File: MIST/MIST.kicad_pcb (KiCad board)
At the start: 2 copper layers, 10 x 10 mm, 2 parts

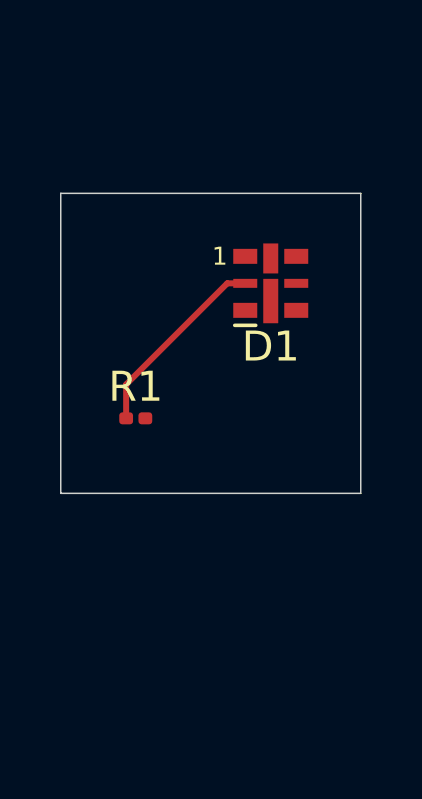
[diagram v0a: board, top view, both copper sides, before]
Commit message: finished BOM and added resources and started layout
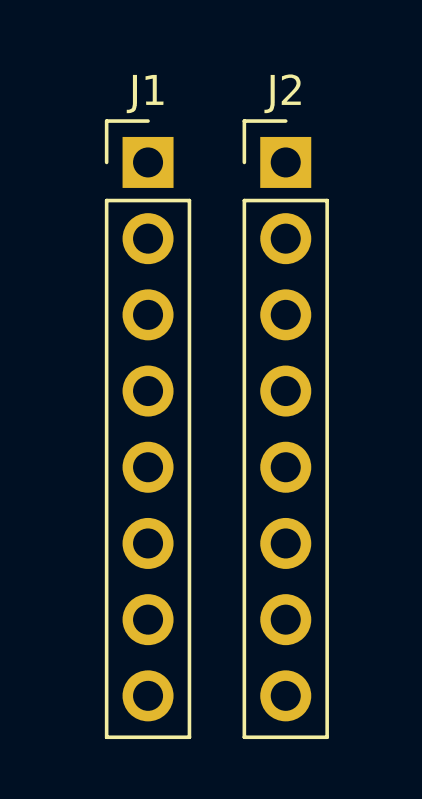
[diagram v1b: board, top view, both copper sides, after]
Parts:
- removed D1: LED, LED_SMD:LED-APA102-2020
- removed R1: 220, Resistor_SMD:R_0201_0603Metric
- added J1: Conn_01x08, Connector_PinHeader_2.54mm:PinHeader_1x08_P2.54mm_Vertical, F.Cu at (140.9, 88.0)
- added J2: Conn_01x08, Connector_PinHeader_2.54mm:PinHeader_1x08_P2.54mm_Vertical, F.Cu at (145.5, 88.0)
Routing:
- net /LED_Anode: track 6.50 -> 0.00 mm
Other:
- board outline removed

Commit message: finished schematic. updated BOM. stuff.
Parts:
- added C1: 100n, Capacitor_SMD:C_0805_2012Metric, F.Cu at (163.8, 39.0)
- added C2: 100n, Capacitor_SMD:C_0805_2012Metric, F.Cu at (163.8, 42.0)
- added C3: 22pF, Capacitor_SMD:C_0805_2012Metric, F.Cu at (163.8, 45.0)
- added C4: 22pF, Capacitor_SMD:C_0805_2012Metric, F.Cu at (163.8, 48.0)
- added C5: 22uF, Capacitor_SMD:C_0805_2012Metric, F.Cu at (163.8, 51.0)
- added J3: USB_C_Receptacle_PowerOnly_6P, Connector_USB:USB_C_Receptacle_GCT_USB4125-xx-x_6P_TopMnt_Horizontal, F.Cu at (179.0, 57.8)
- added J4: ICSP, Connector_PinHeader_2.54mm:PinHeader_2x03_P2.54mm_Vertical, F.Cu at (156.5, 63.5)
- added MK1: CMC-5042PF-AC, CMC-5042PF-AC:CUI_CMC-5042PF-AC, F.Cu at (138.0, 59.2)
- added R1: 10k, Resistor_SMD:R_1206_3216Metric, F.Cu at (181.0, 38.2)
- added R4: 5.1k, Resistor_SMD:R_1206_3216Metric, F.Cu at (181.0, 41.6)
- added R5: 5.1k, Resistor_SMD:R_1206_3216Metric, F.Cu at (181.0, 44.9)
- added S1: SKRPABE010, SKRPABE010:SW_SKRPABE010, F.Cu at (123.2, 62.8)
- added S2: SKRPABE010, SKRPABE010:SW_SKRPABE010, F.Cu at (123.2, 72.5)
- added U1: ATmega328PB-A, Package_QFP:TQFP-32_7x7mm_P0.8mm, F.Cu at (143.1, 48.4)
- added U3: MAX4466EXK, MAX4466EXK:SOT65P210X110-5N, F.Cu at (137.0, 75.2)
- added Y1: 16 Mhz Crystal, Crystal:Crystal_SMD_3225-4Pin_3.2x2.5mm, F.Cu at (151.7, 36.1)
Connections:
- J1 pad 1: unconnected-(J1-Pin_1-Pad1) -> /COL1 (P13)
- J1 pad 2: unconnected-(J1-Pin_2-Pad2) -> /COL2 (P3)
- J1 pad 3: unconnected-(J1-Pin_3-Pad3) -> /COL3 (P4)
- J1 pad 4: unconnected-(J1-Pin_4-Pad4) -> /COL4 (P10)
- J1 pad 5: unconnected-(J1-Pin_5-Pad5) -> /COL5 (P6)
- J1 pad 6: unconnected-(J1-Pin_6-Pad6) -> /COL6 (P11)
- J1 pad 7: unconnected-(J1-Pin_7-Pad7) -> /COL7 (P15)
- J1 pad 8: unconnected-(J1-Pin_8-Pad8) -> /COL8 (P16)
- J2 pad 1: unconnected-(J2-Pin_1-Pad1) -> /ROW1 (P9)
- J2 pad 2: unconnected-(J2-Pin_2-Pad2) -> /ROW2 (P14)
- J2 pad 3: unconnected-(J2-Pin_3-Pad3) -> /ROW3 (P8)
- J2 pad 4: unconnected-(J2-Pin_4-Pad4) -> /ROW4 (P12)
- J2 pad 5: unconnected-(J2-Pin_5-Pad5) -> /ROW5 (P1)
- J2 pad 6: unconnected-(J2-Pin_6-Pad6) -> /ROW6 (P7)
- J2 pad 7: unconnected-(J2-Pin_7-Pad7) -> /ROW7 (P2)
- J2 pad 8: unconnected-(J2-Pin_8-Pad8) -> /ROW8 (P5)

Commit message: finished schematic and layout
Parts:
- added C6: 0.1u, Capacitor_SMD:C_0805_2012Metric, F.Cu at (195.3, 95.8)
- added C7: 0.1n, Capacitor_SMD:C_0805_2012Metric, F.Cu at (195.3, 99.8)
- added C8: 0.1u, Capacitor_SMD:C_0805_2012Metric, F.Cu at (195.3, 103.8)
- added C9: 0.1u, Capacitor_SMD:C_0805_2012Metric, F.Cu at (172.0, 92.2)
- added G***: LOGO, LOGO, F.Cu at (195.8, 110.5)
- added G***: LOGO, LOGO, B.Cu at (154.5, 99.8)
- added G***: LOGO, LOGO, B.Cu at (199.0, 110.5)
- added G***: LOGO, LOGO, B.Cu at (204.0, 100.5)
- added R10: 100k, Resistor_SMD:R_0805_2012Metric, F.Cu at (189.8, 109.5)
- added R2: 10k, Resistor_SMD:R_0805_2012Metric, F.Cu at (189.8, 89.8)
- added R3: 10k, Capacitor_SMD:C_0805_2012Metric, F.Cu at (176.9, 92.2)
- added R6: 2k, Resistor_SMD:R_0805_2012Metric, F.Cu at (189.8, 93.7)
- added R7: 2k, Resistor_SMD:R_0805_2012Metric, F.Cu at (189.8, 97.8)
- added R8: 1M, Resistor_SMD:R_0805_2012Metric, F.Cu at (189.9, 101.5)
- added R9: 1M, Resistor_SMD:R_0805_2012Metric, F.Cu at (189.9, 105.5)
- added U2: MAX7219, Package_SO:SOIC-24W_7.5x15.4mm_P1.27mm, F.Cu at (174.0, 100.0)
- moved S2 89.9 mm to (205.0, 110.0)
- moved S1 89.8 mm to (205.0, 100.0)
- moved R4 76.9 mm to (147.0, 110.5)
- moved MK1 73.7 mm to (205.0, 90.0)
- moved R5 71.1 mm to (147.0, 107.2)
- moved Y1 65.7 mm to (146.9, 101.7)
- moved C1 64.0 mm to (162.7, 103.0), turned to 180 degrees
- moved J3 63.9 mm to (139.2, 107.8), turned to -90 degrees
- moved U3 60.6 mm to (195.8, 90.0)
- moved R1 59.9 mm to (155.0, 92.2)
- moved C2 58.0 mm to (162.7, 100.0), turned to 180 degrees
- moved C3 54.0 mm to (147.5, 96.5), turned to 90 degrees
- moved U1 52.9 mm to (155.0, 100.0)
- moved C4 52.1 mm to (144.5, 96.5), turned to -90 degrees
- moved C5 44.4 mm to (147.5, 92.3), turned to -90 degrees
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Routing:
- net +5V: track 0.00 -> 117.9 mm, vias 0 -> 10
- net /!RESET: track 0.00 -> 88.9 mm, vias 0 -> 2
- net /SWITCHMODE: track 0.00 -> 62.2 mm
- net /ADC0: track 0.00 -> 57.7 mm, vias 0 -> 3
- net /SCK: track 0.00 -> 55.3 mm, vias 0 -> 2
- net Net-(U3-IN+): track 0.00 -> 47.6 mm, vias 0 -> 2
- net GND: track 0.00 -> 45.2 mm, vias 0 -> 20
- net /MOSI: track 0.00 -> 32.1 mm, vias 0 -> 3
- net /MISO: track 0.00 -> 29.1 mm
- net /SS: track 0.00 -> 29.0 mm, vias 0 -> 2
- net Net-(U3-IN-): track 0.00 -> 28.7 mm, vias 0 -> 3
- net /ROW2 (P14): track 0.00 -> 26.7 mm
- net /COL3 (P4): track 0.00 -> 19.9 mm, vias 0 -> 2
- net /COL2 (P3): track 0.00 -> 16.9 mm
- net /COL8 (P16): track 0.00 -> 16.2 mm
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- added copper zone on F.Cu, net GND
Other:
- board outline added: 75.5 x 30.8 mm
- board text added: "1"
- board text added: "MIST"
- board text added: "Mode 1: Talk with MIST Mode 2: Sound visualizer. Play music to the microphone and watch the lights go"
- board text added: "Orientation -> Pin 1 Here"
- board text added: "Play Music Here!"
- board text added: "Reset"
- board text added: "Switch Mode"

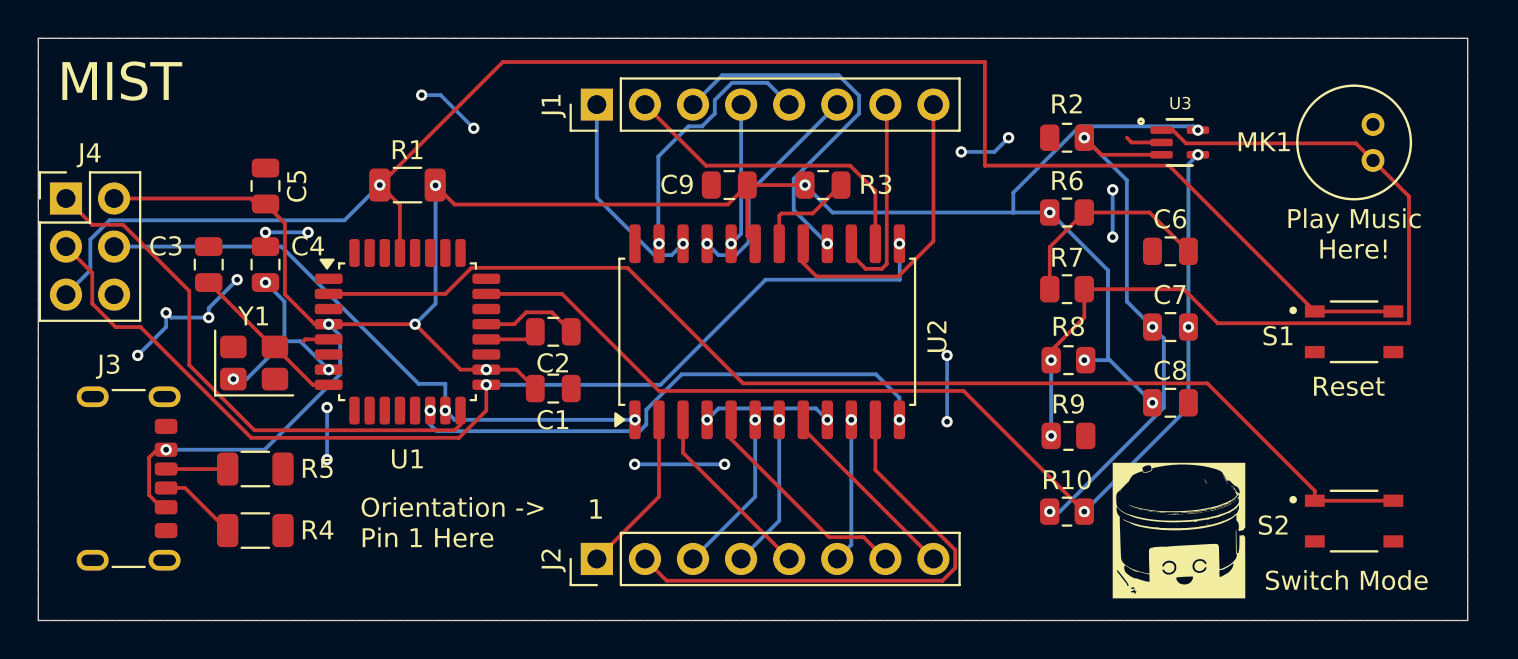
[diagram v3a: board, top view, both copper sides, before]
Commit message: added GND planes to both layers and via stitched
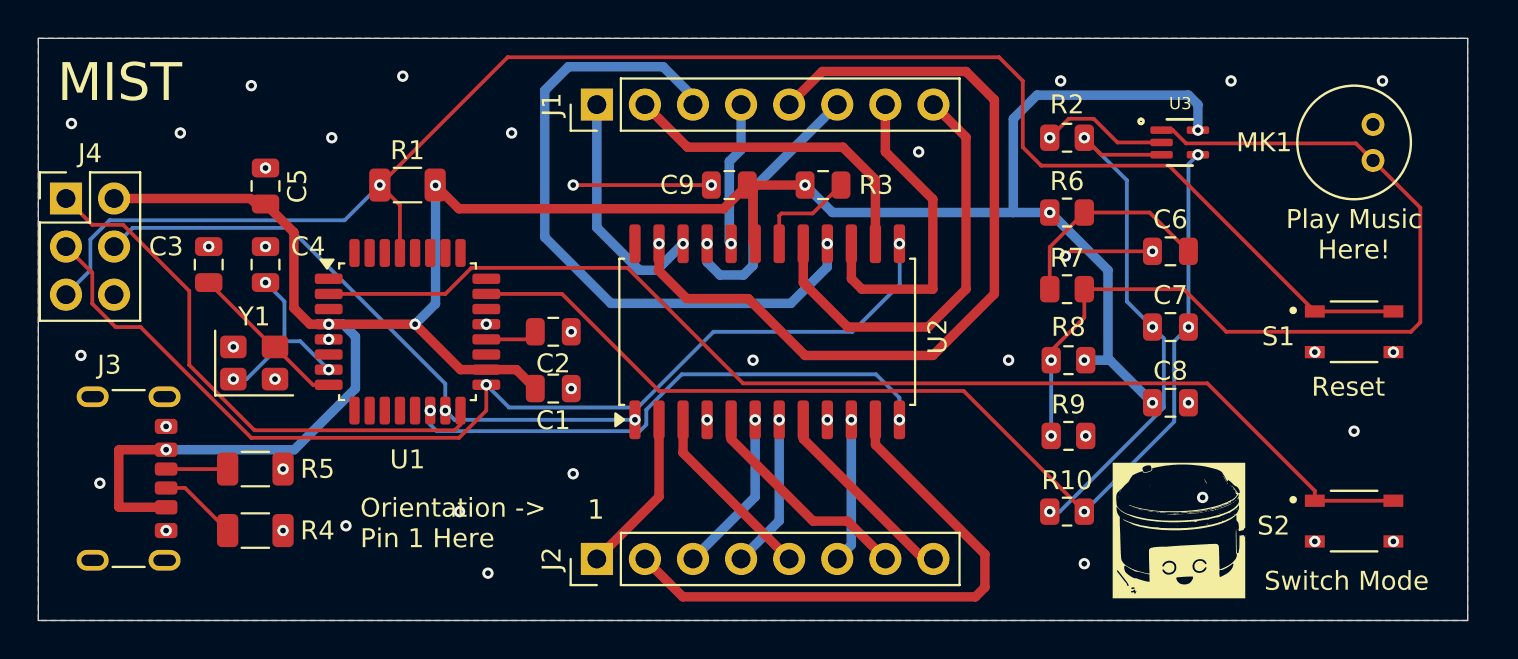
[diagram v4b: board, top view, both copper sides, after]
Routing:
- net /COL5 (P6): track 14.0 -> 44.8 mm
- net GND: track 45.2 -> 18.8 mm, vias 20 -> 53
- net /COL3 (P4): track 19.9 -> 35.6 mm
- net +5V: track 117.9 -> 128.5 mm, vias 10 -> 9
- net /COL8 (P16): track 16.2 -> 22.9 mm
- net /COL7 (P15): track 11.3 -> 17.2 mm
- net /ROW2 (P14): track 26.7 -> 30.2 mm
- net /COL6 (P11): track 11.9 -> 14.2 mm
- net /COL1 (P13): track 11.0 -> 12.6 mm
- net Net-(U3-IN+): track 47.6 -> 48.8 mm
- net /SCK: track 55.3 -> 56.5 mm
- net /!RESET: track 88.9 -> 87.9 mm
- net /MOSI: track 32.1 -> 33.0 mm
- added copper zone on B.Cu, net GND

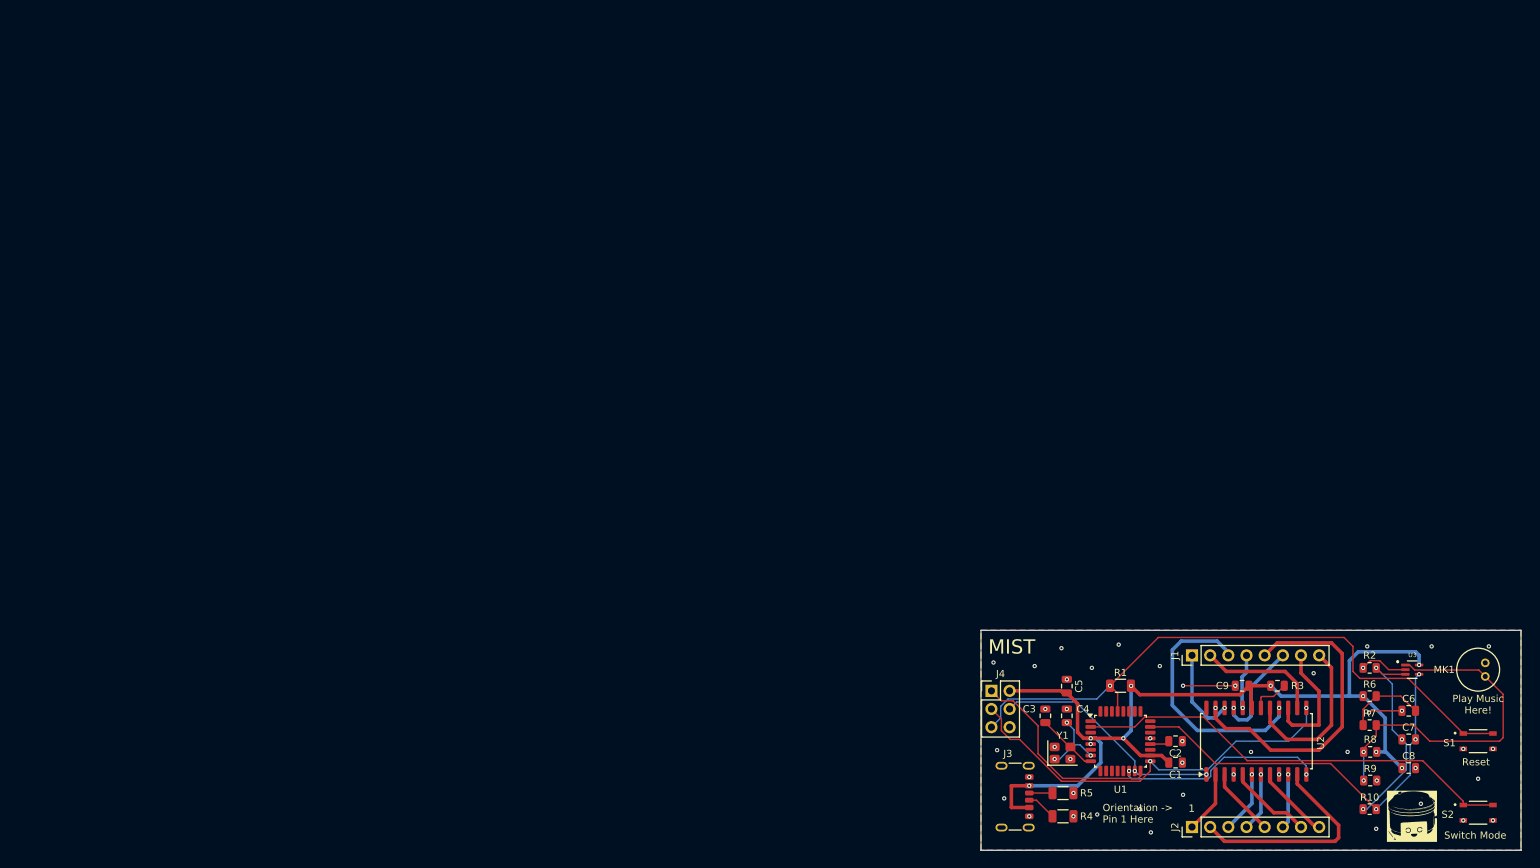
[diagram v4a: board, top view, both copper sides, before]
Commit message: fixed wrong matrix pin mappings schematic.
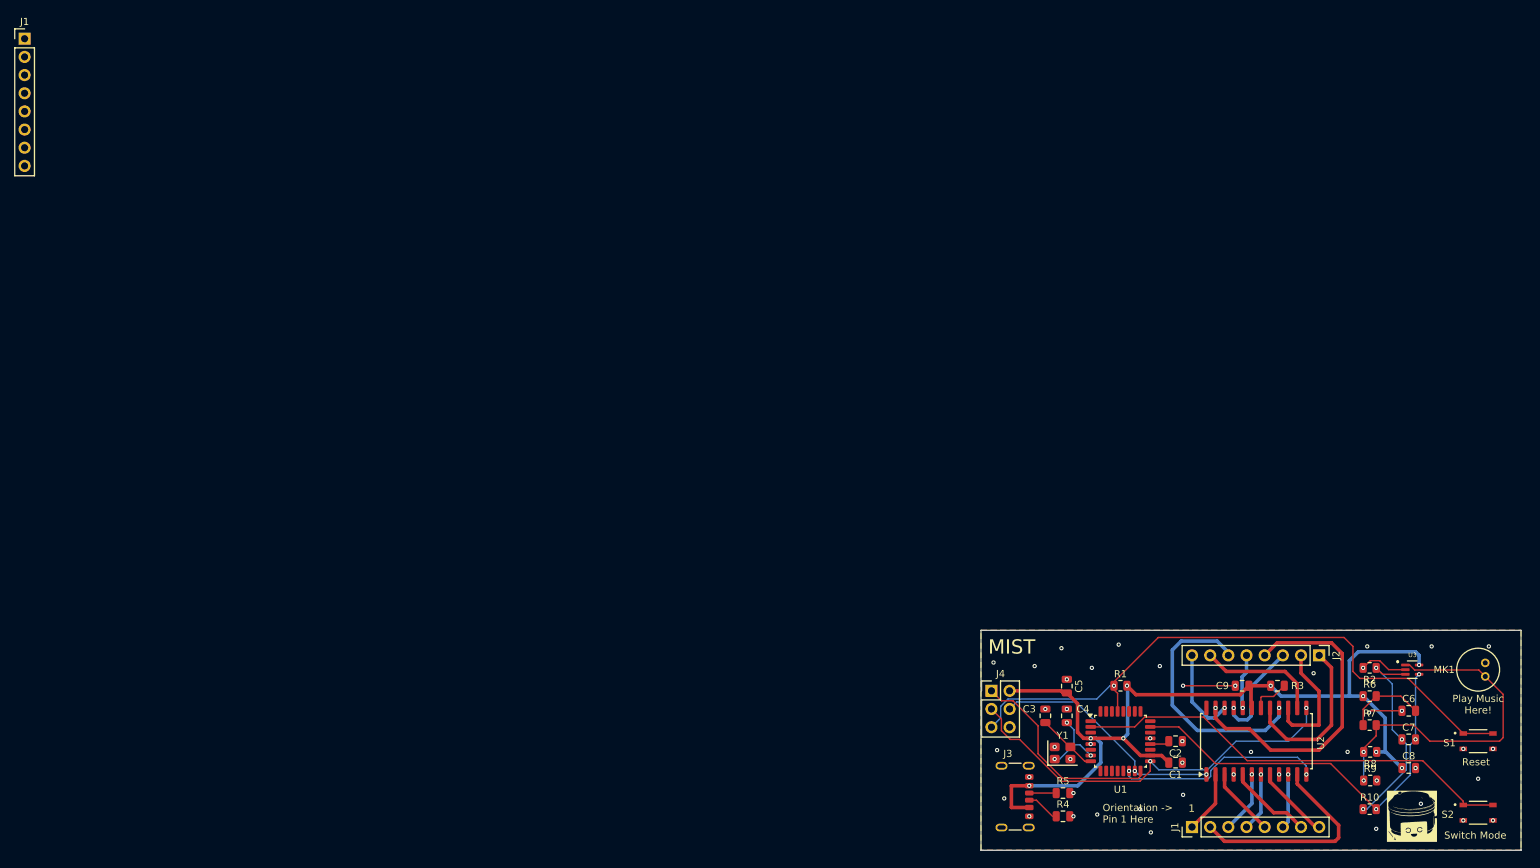
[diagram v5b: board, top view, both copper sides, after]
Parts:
- removed the J1 at (165.0, 88.0)
- added J1: Conn_01x08, Connector_PinHeader_2.54mm:PinHeader_1x08_P2.54mm_Vertical, F.Cu at (1.79, 1.79)
- added J1: Conn_01x08, Connector_PinHeader_2.54mm:PinHeader_1x08_P2.54mm_Vertical, F.Cu at (165.0, 112.0)
- R1: footprint Resistor_SMD:R_1206_3216Metric -> Resistor_SMD:R_0805_2012Metric
- R4, R5: footprint Resistor_SMD:R_1206_3216Metric -> Capacitor_SMD:C_0805_2012Metric
- moved J2 29.9 mm to (182.8, 88.0), turned to -90 degrees
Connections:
- J2 pad 1: /ROW1 (P9) -> (no net)
- J2 pad 2: /ROW2 (P14) -> (no net)
- J2 pad 3: /ROW3 (P8) -> (no net)
- J2 pad 4: /ROW4 (P12) -> (no net)
- J2 pad 5: /ROW5 (P1) -> (no net)
- J2 pad 6: /ROW6 (P7) -> (no net)
- J2 pad 7: /ROW7 (P2) -> (no net)
- J2 pad 8: /ROW8 (P5) -> (no net)

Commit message: fixed matrix pin mappings on layout. updated bitmap silkscreens.
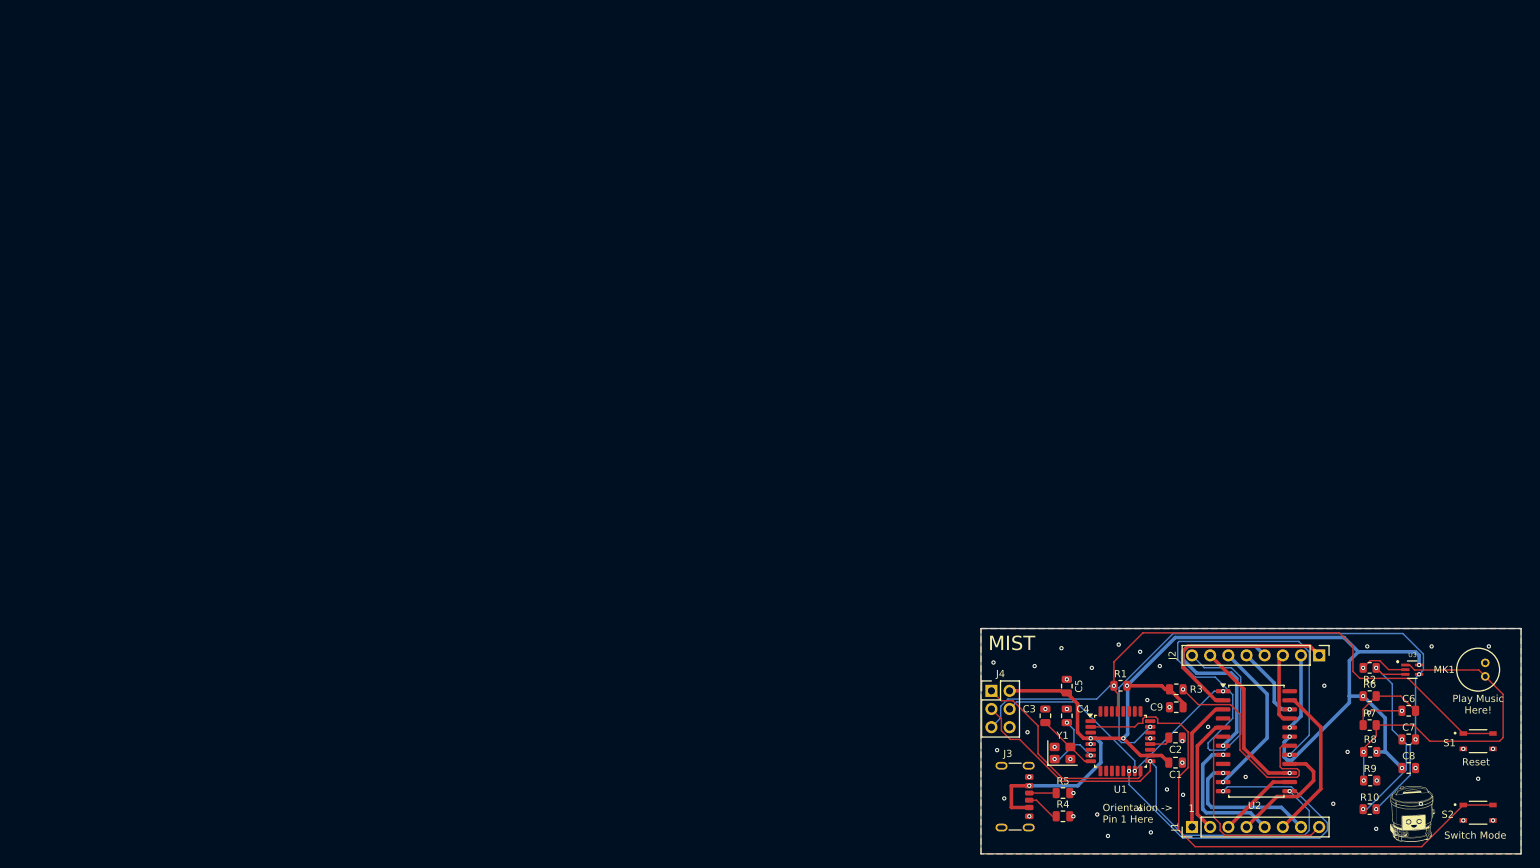
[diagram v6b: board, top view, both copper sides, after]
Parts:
- removed the J1 at (1.79, 1.79)
- moved R3 14.2 mm to (162.8, 92.8)
- moved C9 9.68 mm to (162.8, 95.2)
- moved C2 0.50 mm to (162.7, 99.5)
- moved G*** 0.25 mm to (195.8, 110.2)
- turned U2 to 0 degrees
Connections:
- J1 pad 1: (no net) -> /ROW5 (P1)
- J1 pad 2: (no net) -> /ROW7 (P2)
- J1 pad 3: (no net) -> /COL2 (P3)
- J1 pad 4: (no net) -> /COL3 (P4)
- J1 pad 5: (no net) -> /ROW8 (P5)
- J1 pad 6: (no net) -> /COL5 (P6)
- J1 pad 7: (no net) -> /ROW6 (P7)
- J1 pad 8: (no net) -> /ROW3 (P8)
- J2 pad 1: (no net) -> /ROW1 (P9)
- J2 pad 2: (no net) -> /COL4 (P10)
- J2 pad 3: (no net) -> /COL6 (P11)
- J2 pad 4: (no net) -> /ROW4 (P12)
- J2 pad 5: (no net) -> /COL1 (P13)
- J2 pad 6: (no net) -> /ROW2 (P14)
- J2 pad 7: (no net) -> /COL7 (P15)
- J2 pad 8: (no net) -> /COL8 (P16)
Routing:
- net /COL8 (P16): track 22.9 -> 77.3 mm, vias 0 -> 1
- net Net-(U2-ISET): track 5.42 -> 32.0 mm, vias 0 -> 1
- net /ADC0: track 57.7 -> 84.0 mm, vias 3 -> 4
- net +5V: track 129.0 -> 154.6 mm
- net /ROW4 (P12): track 8.18 -> 32.2 mm, vias 2 -> 1
- net /COL5 (P6): track 44.8 -> 22.1 mm, vias 2 -> 0
- net /SS: track 29.0 -> 51.2 mm
- net /ROW1 (P9): track 8.71 -> 29.7 mm
- net /ROW3 (P8): track 8.71 -> 29.2 mm, vias 2 -> 0
- net /COL3 (P4): track 35.6 -> 17.1 mm, vias 2 -> 0
- net /SWITCHMODE: track 62.2 -> 77.4 mm
- net /ROW6 (P7): track 7.66 -> 20.3 mm, vias 2 -> 1
- net /SCK: track 56.5 -> 66.0 mm
- net /ROW5 (P1): track 9.67 -> 18.8 mm
- net /ROW8 (P5): track 10.5 -> 19.4 mm, vias 0 -> 1
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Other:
- board size 75.5 x 30.8 mm -> 75.5 x 31.5 mm
